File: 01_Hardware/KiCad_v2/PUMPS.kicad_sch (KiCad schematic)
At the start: 20 parts, among them J600 JST_B2B, J601 JST_B2B, Q600 STN3NF06L, Q601 STN3NF06L

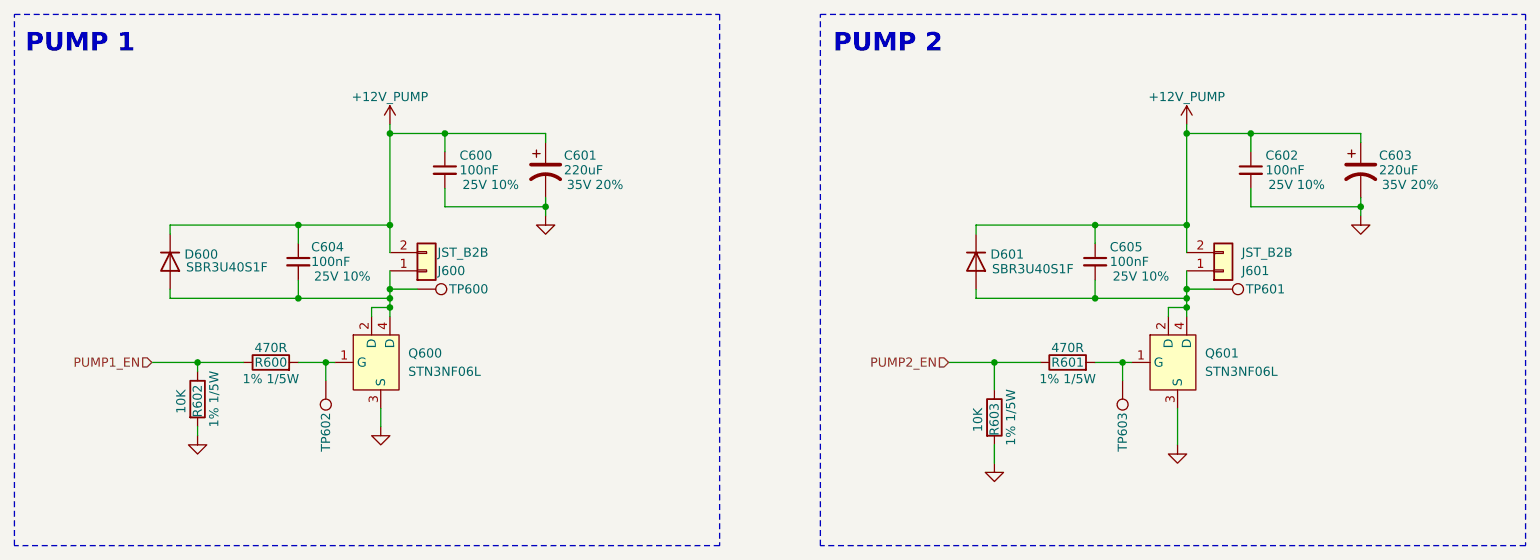
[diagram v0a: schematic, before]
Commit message: BOM done, except connectors/thermistor/button -> Will re-check BOM before sending to manufacturing
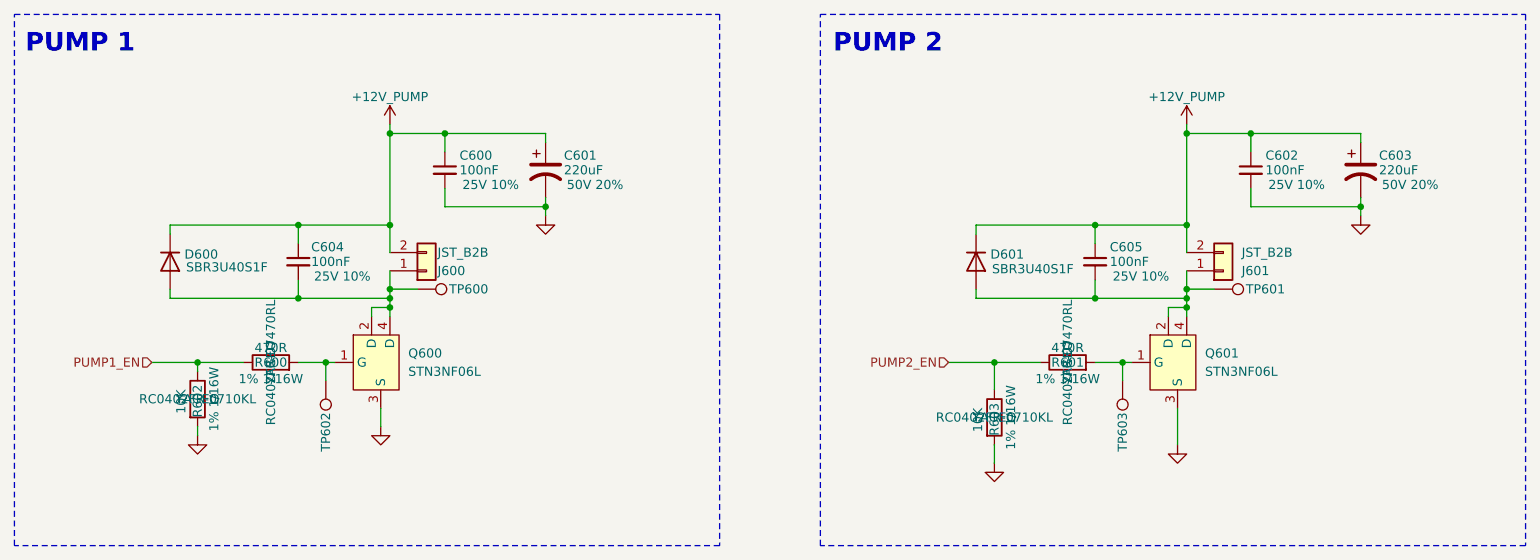
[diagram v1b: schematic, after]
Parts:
- C600, C602, C604, C605: Manufacturer Samsung Electro-Mechanics -> Samsung Electro-Mechanics
- C601, C603: footprint Custom_Global_Footprints:EEEFK1V470P -> Capacitor_SMD:CP_Elec_10x10; Link https://jlcpcb.com/partdetail/PANASONIC-EEEFK1V470P/C178565 -> https://jlcpcb.com/partdetail/Nichicon-UCD1H221MNL1GS/C1162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; Manufacturer Panasonic -> Nichicon; Manufacturer Part Number EEE-FK1V470P -> UCD1H221MNL1GS
- Q600, Q601: Link (none) -> https://jlcpcb.com/partdetail/STMicroelectronics-STN3NF06L/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; Manufacturer (none) -> STMicroelectronics; Manufacturer Part Number (none) -> STN3NF06L
- R600, R601: Manufacturer (none) -> YAGEO; Manufacturer Part Number (none) -> RC0402FR-07470RL
- R602, R603: Manufacturer (none) -> YAGEO; Manufacturer Part Number (none) -> RC0402FR-0710KL
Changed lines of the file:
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@@
 			)
 		)
-		(property "Manufacturer" "Samsung Electro-Mechanics "
+		(property "Manufacturer" "Samsung Electro-Mechanics"
 			(at 85.09 88.9 0)
 			(effects
@@
 			)
 		)
-		(property "Datasheet" "~"
+		(property "Datasheet" ""
 			(at 213.36 90.17 0)
 			(effects
@@
 			)
 		)
-		(property "Description" "1% 1/5W"
+		(property "Description" "1% 1/16W"
 			(at 73.406 107.95 90)
 			(effects
@@
 		)
 		(property "Secound Source" ""
+			(at 71.12 107.95 0)
+			(effects
+				(font
+					(size 1.27 1.27)
+				)
+			)
+		)
+		(property "Manufacturer" "YAGEO"
+			(at 71.12 107.95 0)
+			(effects
+				(font
+					(size 1.27 1.27)
+				)
+			)
+		)
+		(property "Manufacturer Part Number" "RC0402FR-0710KL"
 			(at 71.12 107.95 0)
 			(effects
@@
 			)
 		)
-		(property "Datasheet" "~"
+		(property "Datasheet" ""
 			(at 102.87 90.17 0)
 			(effects
@@
 			)
 		)
-		(property "Manufacturer" "Samsung Electro-Mechanics "
+		(property "Manufacturer" "Samsung Electro-Mechanics"
 			(at 195.58 88.9 0)
 			(effects
@@
 			)
 		)
-		(property "Datasheet" "~"
+		(property "Datasheet" ""
 			(at 81.28 102.87 0)
 			(effects
@@
 			)
 		)
-		(property "Description" "1% 1/5W"
+		(property "Description" "1% 1/16W"
 			(at 81.28 105.156 90)
 			(effects
@@
 		)
 		(property "Secound Source" ""
+			(at 81.28 102.87 0)
+			(effects
+				(font
+					(size 1.27 1.27)
+				)
+			)
+		)
+		(property "Manufacturer" "YAGEO"
+			(at 81.28 102.87 0)
+			(effects
+				(font
+					(size 1.27 1.27)
+				)
+			)
+		)
+		(property "Manufacturer Part Number" "RC0402FR-07470RL"
 			(at 81.28 102.87 0)
 			(effects
@@
 			)
 		)
-		(property "Datasheet" "~"
+		(property "Datasheet" ""
 			(at 204.47 105.41 0)
 			(effects
@@
 			)
 		)
-		(property "Datasheet" "https://eu.mouser.com/ProductDetail/STMicroelectronics/STN3NF06L?qs=VREXnN%2FAp%252BtujmZVCVKGgA%3D%3D&srsltid=AfmBOooDUSGEvTvsGTI3cICKREi36a1JB1pR-TC-y9iQo2YLDLO6qmrY"
+		(property "Datasheet" "https://jlcpcb.com/api/file/downloadByFileSystemAccessId/8588883600968462336"
 			(at 95.25 102.87 0)
 			(effects
@@
 			)
 		)
-		(property "Description" ""
+		(property "Description" "N-Channel 120mΩ@5V 2.8V@250uA 3.3W 30pF 340pF 4A 60V 63pF 9nC@5V N-Channel SOT-223 MOSFETs"
 			(at 95.25 102.87 0)
 			(effects
@@
 					(size 1.27 1.27)
 				)
+				(hide yes)
 			)
 		)
@@
 					(size 1.27 1.27)
 				)
+				(hide yes)
+			)
+		)
+		(property "Link" "https://jlcpcb.com/partdetail/STMicroelectronics-STN3NF06L/C222218"
+			(at 95.25 102.87 0)
+			(effects
+				(font
+					(size 1.27 1.27)
+				)
+				(hide yes)
+			)
+		)
+		(property "Manufacturer" "STMicroelectronics"
+			(at 95.25 102.87 0)
+			(effects
+				(font
+					(size 1.27 1.27)
+				)
+				(hide yes)
+			)
+		)
+		(property "Manufacturer Part Number" "STN3NF06L"
+			(at 95.25 102.87 0)
+			(effects
+				(font
+					(size 1.27 1.27)
+				)
+				(hide yes)
 			)
 		)
@@
 			)
 		)
-		(property "Description" "1% 1/5W"
+		(property "Description" "1% 1/16W"
 			(at 183.896 110.49 90)
 			(effects
@@
 		)
 		(property "Secound Source" ""
+			(at 181.61 110.49 0)
+			(effects
+				(font
+					(size 1.27 1.27)
+				)
+			)
+		)
+		(property "Manufacturer" "YAGEO"
+			(at 181.61 110.49 0)
+			(effects
+				(font
+					(size 1.27 1.27)
+				)
+			)
+		)
+		(property "Manufacturer Part Number" "RC0402FR-0710KL"
 			(at 181.61 110.49 0)
 			(effects
@@
 			)
 		)
-		(property "Datasheet" "~"
+		(property "Datasheet" ""
 			(at 101.6 87.63 0)
 			(effects
@@
 			)
 		)
-		(property "Datasheet" "~"
+		(property "Datasheet" ""
 			(at 93.98 105.41 0)
 			(effects
@@
 			)
 		)
-		(property "Manufacturer" "Samsung Electro-Mechanics "
+		(property "Manufacturer" "Samsung Electro-Mechanics"
 			(at 105.41 76.2 0)
 			(effects
@@
 			)
 		)
-		(property "Footprint" "Custom_Global_Footprints:EEEFK1V470P"
+		(property "Footprint" "Capacitor_SMD:CP_Elec_10x10"
 			(at 232.41 76.2 0)
 			(effects
@@
 			)
 		)
-		(property "Datasheet" "https://jlcpcb.com/api/file/downloadByFileSystemAccessId/8588893102903316480"
+		(property "Datasheet" "https://jlcpcb.com/api/file/downloadByFileSystemAccessId/8588899068991324160"
 			(at 232.41 76.2 0)
 			(effects
@@
 			)
 		)
-		(property "Description" "35V 20%"
+		(property "Description" "50V 20%"
 			(at 239.268 78.232 0)
 			(effects
@@
 			)
 		)
-		(property "Manufacturer" "Panasonic"
+		(property "Manufacturer" "Nichicon"
 			(at 232.41 76.2 0)
 			(effects
@@
 			)
 		)
-		(property "Manufacturer Part Number" "EEE-FK1V470P"
+		(property "Manufacturer Part Number" "UCD1H221MNL1GS"
 			(at 232.41 76.2 0)
 			(effects
@@
 			)
 		)
-		(property "Link" "https://jlcpcb.com/partdetail/PANASONIC-EEEFK1V470P/C178565"
+		(property "Link" "https://jlcpcb.com/partdetail/Nichicon-UCD1H221MNL1GS/C116211"
 			(at 232.41 76.2 0)
 			(effects
@@
 			)
 		)
-		(property "Datasheet" "https://eu.mouser.com/ProductDetail/STMicroelectronics/STN3NF06L?qs=VREXnN%2FAp%252BtujmZVCVKGgA%3D%3D&srsltid=AfmBOooDUSGEvTvsGTI3cICKREi36a1JB1pR-TC-y9iQo2YLDLO6qmrY"
+		(property "Datasheet" "https://jlcpcb.com/api/file/downloadByFileSystemAccessId/8588883600968462336"
 			(at 205.74 102.87 0)
 			(effects
@@
 			)
 		)
-		(property "Description" ""
+		(property "Description" "N-Channel 120mΩ@5V 2.8V@250uA 3.3W 30pF 340pF 4A 60V 63pF 9nC@5V N-Channel SOT-223 MOSFETs"
 			(at 205.74 102.87 0)
 			(effects
@@
 					(size 1.27 1.27)
 				)
+				(hide yes)
 			)
 		)
@@
 					(size 1.27 1.27)
 				)
+				(hide yes)
+			)
+		)
+		(property "Link" "https://jlcpcb.com/partdetail/STMicroelectronics-STN3NF06L/C222218"
+			(at 205.74 102.87 0)
+			(effects
+				(font
+					(size 1.27 1.27)
+				)
+				(hide yes)
+			)
+		)
+		(property "Manufacturer" "STMicroelectronics"
+			(at 205.74 102.87 0)
+			(effects
+				(font
+					(size 1.27 1.27)
+				)
+				(hide yes)
+			)
+		)
+		(property "Manufacturer Part Number" "STN3NF06L"
+			(at 205.74 102.87 0)
+			(effects
+				(font
+					(size 1.27 1.27)
+				)
+				(hide yes)
 			)
 		)
@@
 			)
 		)
-		(property "Datasheet" "~"
+		(property "Datasheet" ""
 			(at 212.09 87.63 0)
 			(effects
@@
 			)
 		)
-		(property "Footprint" "Custom_Global_Footprints:EEEFK1V470P"
+		(property "Footprint" "Capacitor_SMD:CP_Elec_10x10"
 			(at 119.38 76.2 0)
 			(effects
@@
 			)
 		)
-		(property "Datasheet" "https://jlcpcb.com/api/file/downloadByFileSystemAccessId/8588893102903316480"
+		(property "Datasheet" "https://jlcpcb.com/api/file/downloadByFileSystemAccessId/8588899068991324160"
 			(at 119.38 76.2 0)
 			(effects
@@
 			)
 		)
-		(property "Description" "35V 20%"
+		(property "Description" "50V 20%"
 			(at 126.238 78.232 0)
 			(effects
@@
 			)
 		)
-		(property "Manufacturer" "Panasonic"
+		(property "Manufacturer" "Nichicon"
 			(at 119.38 76.2 0)
 			(effects
@@
 			)
 		)
-		(property "Manufacturer Part Number" "EEE-FK1V470P"
+		(property "Manufacturer Part Number" "UCD1H221MNL1GS"
 			(at 119.38 76.2 0)
 			(effects
@@
 			)
 		)
-		(property "Link" "https://jlcpcb.com/partdetail/PANASONIC-EEEFK1V470P/C178565"
+		(property "Link" "https://jlcpcb.com/partdetail/Nichicon-UCD1H221MNL1GS/C116211"
 			(at 119.38 76.2 0)
 			(effects
@@
 			)
 		)
-		(property "Manufacturer" "Samsung Electro-Mechanics "
+		(property "Manufacturer" "Samsung Electro-Mechanics"
 			(at 217.17 76.2 0)
 			(effects
@@
 			)
 		)
-		(property "Datasheet" "~"
+		(property "Datasheet" ""
 			(at 191.77 102.87 0)
 			(effects
@@
 			)
 		)
-		(property "Description" "1% 1/5W"
+		(property "Description" "1% 1/16W"
 			(at 191.77 105.156 90)
 			(effects
@@
 			(at 191.77 102.87 0)
 			(effects
+				(font
+					(size 1.27 1.27)
+				)
+			)
+		)
+		(property "Manufacturer" "YAGEO"
+			(at 191.77 102.87 0)
+			(effects
+				(font
+					(size 1.27 1.27)
+				)
+			)
+		)
+		(property "Manufacturer Part Number" "RC0402FR-07470RL"
+			(at 191.77 102.87 0)
+			(effects

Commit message: USB-C and Serial PCB routing done
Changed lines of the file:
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@@
 					(size 1.27 1.27)
 				)
+				(hide yes)
 			)
 		)
@@
 					(size 1.27 1.27)
 				)
+				(hide yes)
 			)
 		)
@@
 					(size 1.27 1.27)
 				)
+				(hide yes)
 			)
 		)
@@
 					(size 1.27 1.27)
 				)
+				(hide yes)
 			)
 		)
@@
 					(size 1.27 1.27)
 				)
+				(hide yes)
 			)
 		)
@@
 					(size 1.27 1.27)
 				)
+				(hide yes)
 			)
 		)
@@
 					(size 1.27 1.27)
 				)
+				(hide yes)
 			)
 		)
@@
 					(size 1.27 1.27)
 				)
+				(hide yes)
 			)
 		)
@@
 					(size 1.27 1.27)
 				)
+				(hide yes)
 			)
 		)
@@
 					(size 1.27 1.27)
 				)
+				(hide yes)
 			)
 		)
@@
 					(size 1.27 1.27)
 				)
+				(hide yes)
 			)
 		)
@@
 					(size 1.27 1.27)
 				)
+				(hide yes)
 			)
 		)
@@
 					(size 1.27 1.27)
 				)
+				(hide yes)
 			)
 		)
@@
 					(size 1.27 1.27)
 				)
+				(hide yes)
 			)
 		)
@@
 					(size 1.27 1.27)
 				)
+				(hide yes)
 			)
 		)
@@
 					(size 1.27 1.27)
 				)
-			)
-		)
+				(hide yes)
+			)
+		)

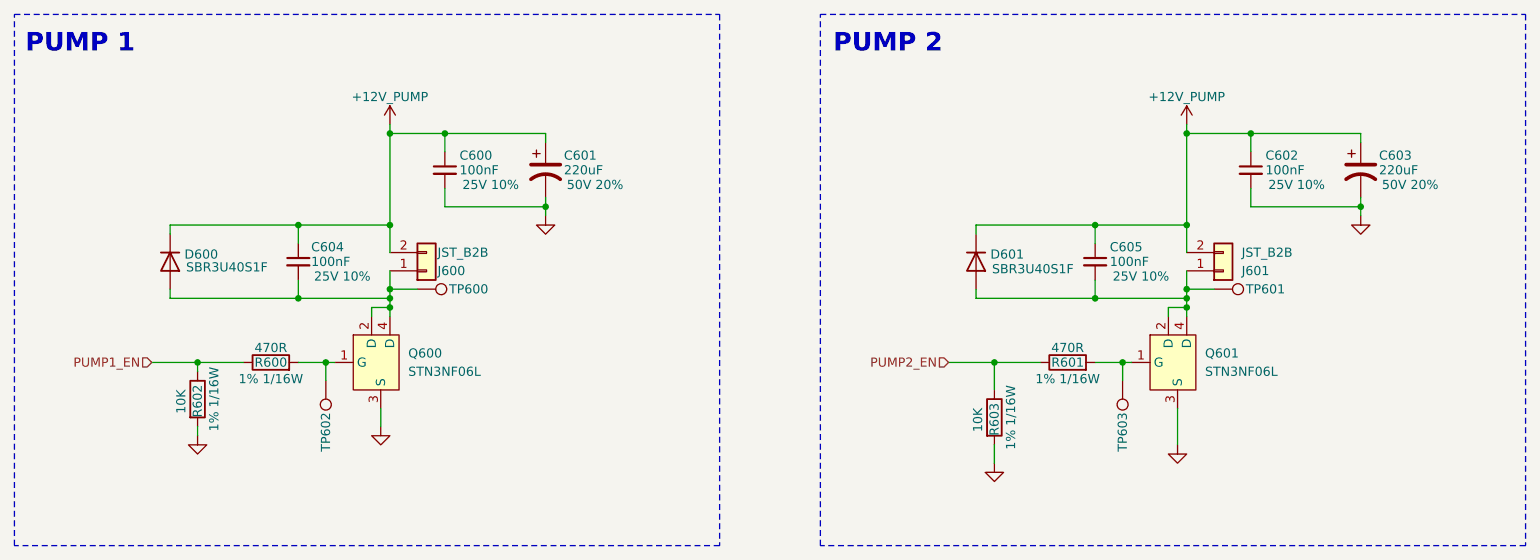
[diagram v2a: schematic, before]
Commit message: Power plane/rearranged connectors
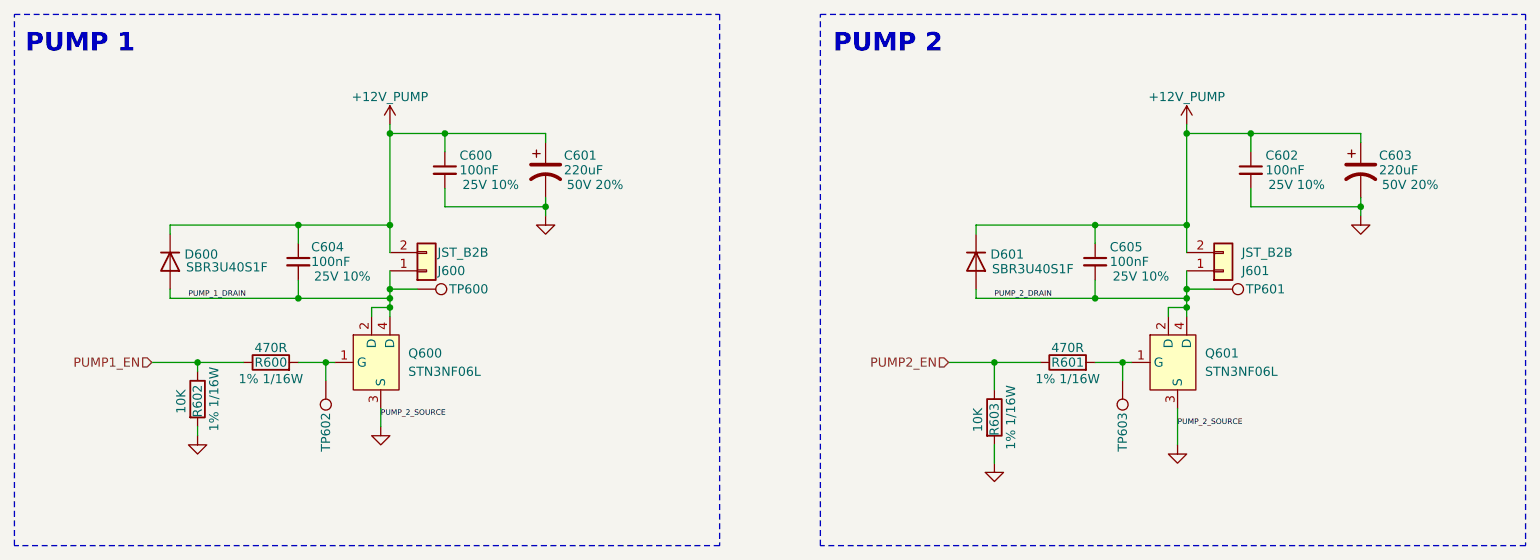
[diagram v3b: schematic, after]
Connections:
- net PUMP_1_DRAIN: now reaches C604.2, D600.2 (A), J600.1 (Pin_1), Q600.2 (D), Q600.4 (D), TP600.1
- net PUMP_2_DRAIN: now reaches C605.2, D601.2 (A), J601.1 (Pin_1), Q601.2 (D), Q601.4 (D), TP601.1
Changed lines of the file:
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@@
+		)
+	)
+	(label "PUMP_2_SOURCE"
+		(at 207.01 111.76 0)
+		(effects
+			(font
+				(size 0.762 0.762)
+			)
+			(justify left bottom)
+		)
+	)
+	(label "PUMP_2_DRAIN"
+		(at 181.61 93.98 0)
+		(effects
+			(font
+				(size 0.762 0.762)
+			)
+			(justify left bottom)
+		)
+	)
+	(label "PUMP_2_SOURCE"
+		(at 96.52 110.49 0)
+		(effects
+			(font
+				(size 0.762 0.762)
+			)
+			(justify left bottom)
+		)
+	)
+	(label "PUMP_1_DRAIN"
+		(at 69.85 93.98 0)
+		(effects
+			(font
+				(size 0.762 0.762)
+			)
+			(justify left bottom)
 		)
 	)
